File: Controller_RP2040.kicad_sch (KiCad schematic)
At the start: 9 parts, among them J2 Conn_ARM_SWD_TagConnect_TC203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, U3 NCP1117-3.3

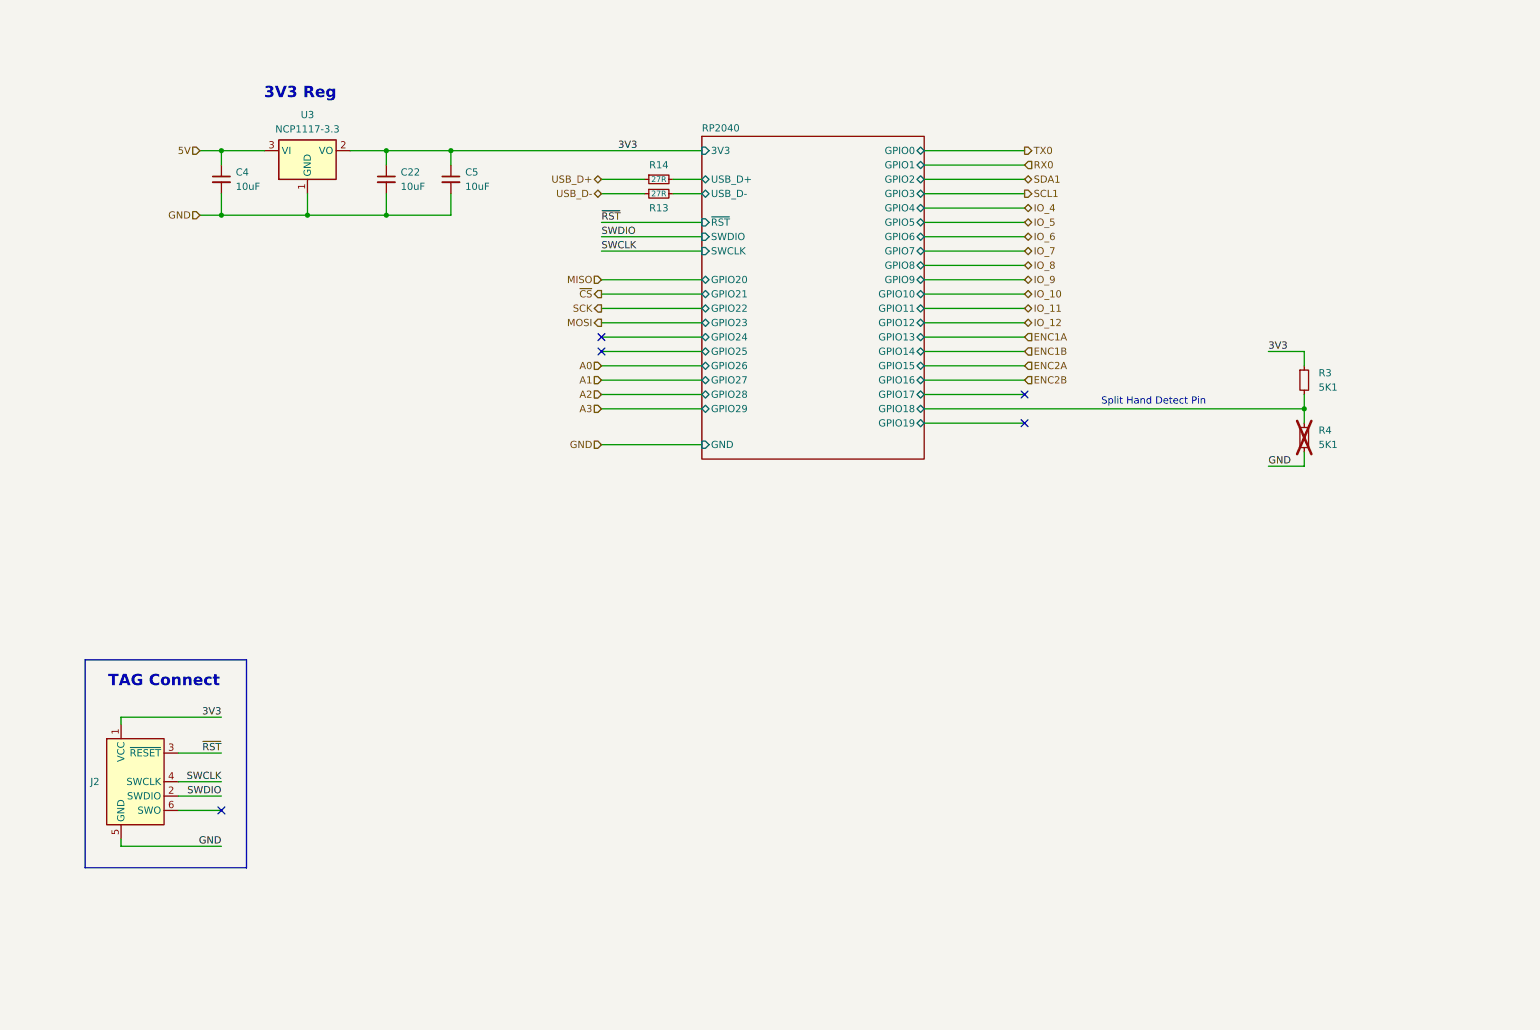
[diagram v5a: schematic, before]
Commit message: Review Schematic, Add TRS connector. Continue routing
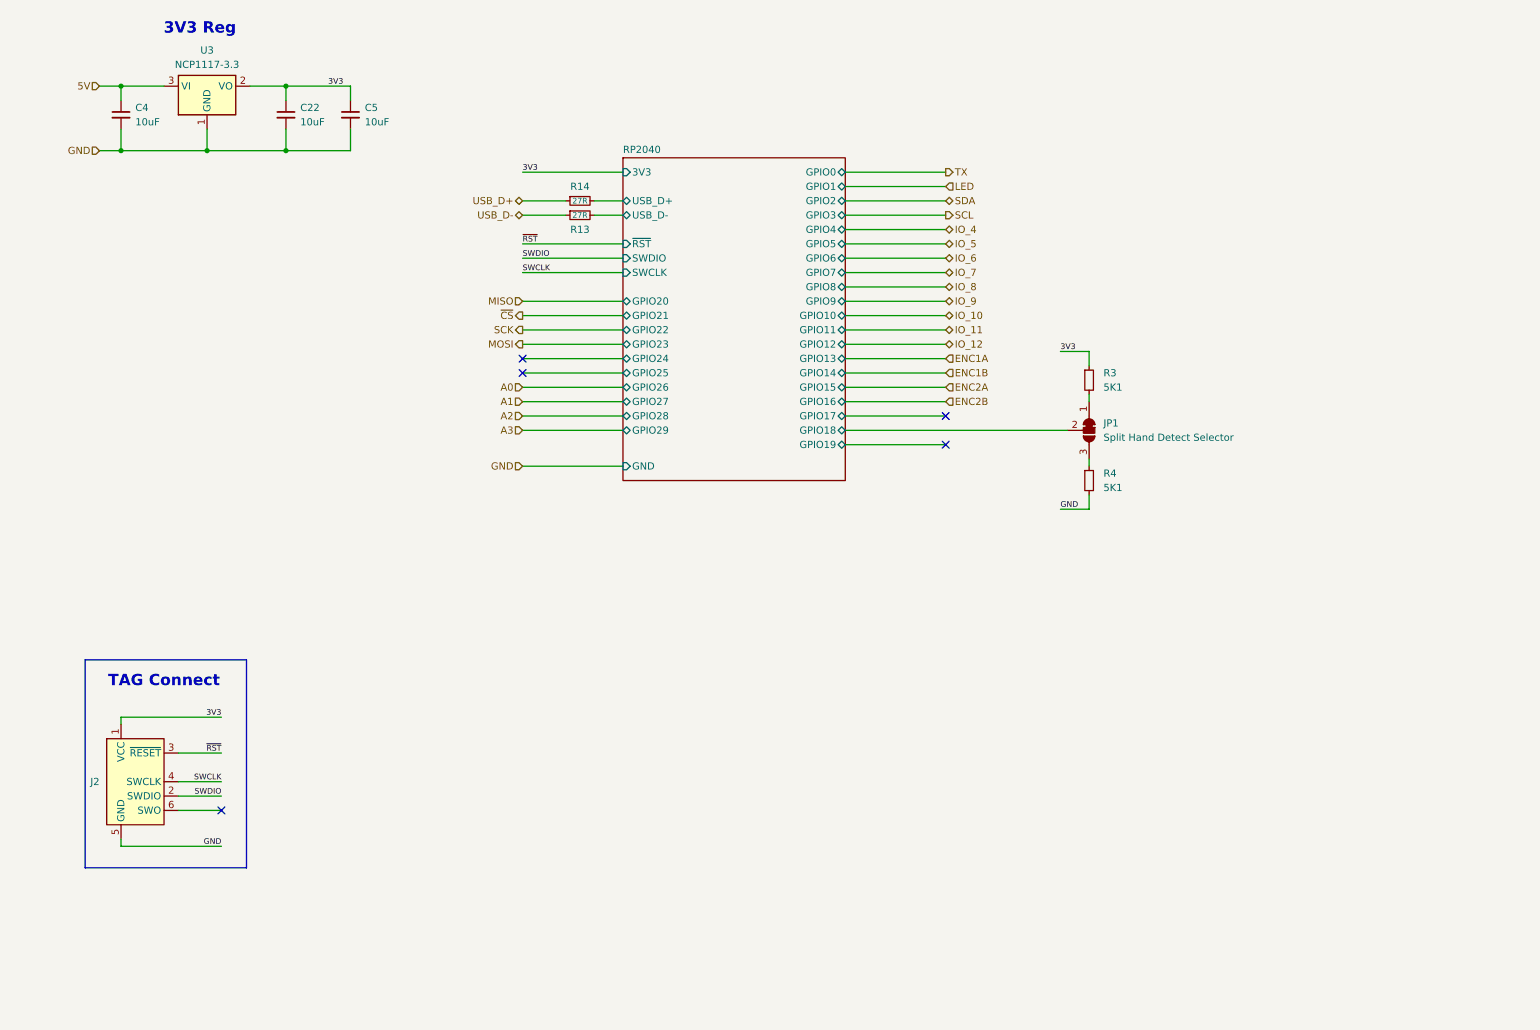
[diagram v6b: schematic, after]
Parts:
- added JP1: Split Hand Detect Selector, Jumper:SolderJumper-3_P1.3mm_Bridged12_RoundedPad1.0x1.5mm, symbol Jumper:SolderJumper_3_Bridged12
- R4: now fitted
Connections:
- net RP2040/GPIO18: now also JP1.2 (C); no longer R3.2, R4.1
- new net: JP1.1 (A), R3.2
- new net: JP1.3 (B), R4.1
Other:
- note removed: "Split Hand Detect Pin"
- moved on the sheet: C22, C4, C5, R13, R14, R3, U3

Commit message: Continue routing.
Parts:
- J2: footprint Connector:Tag-Connect_TC2030-IDC-NL_2x03_P1.27mm_Vertical -> Connector_JST:JST_SHL_SM05B-SHLS-TF_1x05-1MP_P1.00mm_Horizontal; symbol Connector:Conn_ARM_SWD_TagConnect_TC2030-NL -> Connector_Generic_MountingPin:Conn_01x05_MountingPin; now not fitted; now in the parts list
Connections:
- net GND: now also J2.MP (MountPin)
- net SWCLK: now also J2.3 (Pin_3); no longer J2.4 (SWCLK)
- net SWDIO: now also J2.4 (Pin_4); no longer J2.2 (SWDIO)
- net ~{RST}: now also J2.2 (Pin_2); no longer J2.3 (~{RESET})
- no-connect marks 5 -> 4
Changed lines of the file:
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@@
 	(rectangle
 		(start 29.21 132.08)
-		(end 57.785 168.91)
+		(end 57.785 162.56)
 		(stroke
 			(width 0)
@@
 	)
 	(no_connect
-		(at 53.34 158.75)
-	)
-	(no_connect
 		(at 181.61 88.9)
 	)
@@
 	(wire
 		(pts
-			(xy 45.72 156.21) (xy 53.34 156.21)
+			(xy 41.91 149.86) (xy 49.53 149.86)
+		)
+		(stroke
+			(width 0)
+			(type default)
+		)
+	)
+	(wire
+		(pts
+			(xy 36.83 160.02) (xy 48.26 160.02)
 		)
 		(stroke
@@
 	(wire
 		(pts
-			(xy 45.72 153.67) (xy 53.34 153.67)
+			(xy 41.91 147.32) (xy 49.53 147.32)
 		)
 		(stroke
@@
 	(wire
 		(pts
-			(xy 53.34 142.24) (xy 35.56 142.24)
+			(xy 49.53 142.24) (xy 41.91 142.24)
 		)
 		(stroke
@@
 	(wire
 		(pts
+			(xy 41.91 152.4) (xy 49.53 152.4)
+		)
+		(stroke
+			(width 0)
+			(type default)
+		)
+	)
+	(wire
+		(pts
 			(xy 106.68 58.42) (xy 124.46 58.42)
 		)
@@
 	(wire
 		(pts
-			(xy 35.56 142.24) (xy 35.56 143.51)
-		)
-		(stroke
-			(width 0)
-			(type default)
-		)
-	)
-	(wire
-		(pts
 			(xy 35.56 30.48) (xy 35.56 33.02)
 		)
@@
 	(wire
 		(pts
-			(xy 53.34 165.1) (xy 35.56 165.1)
-		)
-		(stroke
-			(width 0)
-			(type default)
-		)
-	)
-	(wire
-		(pts
 			(xy 35.56 30.48) (xy 43.18 30.48)
 		)
@@
 	(wire
 		(pts
-			(xy 45.72 148.59) (xy 53.34 148.59)
+			(xy 41.91 144.78) (xy 49.53 144.78)
 		)
 		(stroke
@@
 	(wire
 		(pts
-			(xy 45.72 158.75) (xy 53.34 158.75)
-		)
-		(stroke
-			(width 0)
-			(type default)
-		)
-	)
-	(wire
-		(pts
 			(xy 163.83 68.58) (xy 181.61 68.58)
 		)
@@
 	(wire
 		(pts
-			(xy 35.56 165.1) (xy 35.56 163.83)
+			(xy 36.83 160.02) (xy 36.83 157.48)
 		)
 		(stroke
@@
 		)
 	)
+	(label "GND"
+		(at 48.26 160.02 180)
+		(effects
+			(font
+				(size 1 1)
+			)
+			(justify right bottom)
+		)
+	)
 	(label "SWDIO"
-		(at 53.34 156.21 180)
+		(at 49.53 149.86 180)
 		(effects
 			(font
@@
 	)
 	(label "~{RST}"
-		(at 53.34 148.59 180)
+		(at 49.53 144.78 180)
 		(effects
 			(font
@@
 	)
 	(label "3V3"
-		(at 53.34 142.24 180)
+		(at 49.53 142.24 180)
 		(effects
 			(font
@@
 	)
 	(label "GND"
-		(at 53.34 165.1 180)
+		(at 49.53 152.4 180)
 		(effects
 			(font
@@
 	)
 	(label "SWCLK"
-		(at 53.34 153.67 180)
+		(at 49.53 147.32 180)
 		(effects
 			(font
@@
 			)
 		)
-		(property "Datasheet" "https://www.yageo.com/upload/media/product/products/datasheet/rchip/PYu-RC_Group_51_RoHS_L_12.pdf"
+		(property "Datasheet" "~"
 			(at 116.84 50.8 0)
 			(effects
@@
 			)
 		)
-		(property "Description" "27 Ohms ±1% 0.063W, 1/16W Chip Resistor 0402 (1005 Metric) Moisture Resistant Thick Film"
+		(property "Description" "Resistor, small symbol"
 			(at 116.84 50.8 0)
 			(effects
@@
 	)
 	(symbol
-		(lib_id "Connector:Conn_ARM_SWD_TagConnect_TC2030-NL")
-		(at 38.1 153.67 0)
+		(lib_id "Connector_Generic_MountingPin:Conn_01x05_MountingPin")
+		(at 36.83 147.32 0)
+		(mirror y)
 		(unit 1)
 		(exclude_from_sim no)
-		(in_bom no)
+		(in_bom yes)
 		(on_board yes)
-		(dnp no)
-		(fields_autoplaced yes)
+		(dnp yes)
 		(property "Reference" "J2"
-			(at 31.75 153.6699 0)
+			(at 34.29 147.3199 0)
+			(effects
+				(font
+					(size 1.27 1.27)
+				)
+				(justify left)
+			)
+		)
+		(property "Value" "Conn_ARM_SWD_TagConnect_TC2030-NL"
+			(at 43.18 148.59 0)
 			(effects
 				(font
@@
 				)
 				(justify right)
-			)
-		)
-		(property "Value" "Conn_ARM_SWD_TagConnect_TC2030-NL"
-			(at 31.75 154.94 0)
-			(effects
-				(font
-					(size 1.27 1.27)
-				)
-				(justify right)
-				(hide yes)
-			)
-		)
-		(property "Footprint" "Connector:Tag-Connect_TC2030-IDC-NL_2x03_P1.27mm_Vertical"
-			(at 38.1 171.45 0)
-			(effects
-				(font
-					(size 1.27 1.27)
-				)
-				(hide yes)
-			)
-		)
-		(property "Datasheet" "https://www.tag-connect.com/wp-content/uploads/bsk-pdf-manager/TC2030-CTX_1.pdf"
-			(at 38.1 168.91 0)
-			(effects
-				(font
-					(size 1.27 1.27)
-				)
-				(hide yes)
-			)
-		)
-		(property "Description" ""
-			(at 38.1 153.67 0)
+				(hide yes)
+			)
+		)
+		(property "Footprint" "Connector_JST:JST_SHL_SM05B-SHLS-TF_1x05-1MP_P1.00mm_Horizontal"
+			(at 36.83 147.32 0)
+			(effects
+				(font
+					(size 1.27 1.27)
+				)
+				(hide yes)
+			)
+		)
+		(property "Datasheet" "~"
+			(at 36.83 147.32 0)
+			(effects
+				(font
+					(size 1.27 1.27)
+				)
+				(hide yes)
+			)
+		)
+		(property "Description" "Generic connectable mounting pin connector, single row, 01x05, script generated (kicad-library-utils/schlib/autogen/connector/)"
+			(at 36.83 147.32 0)
 			(effects
 				(font
@@
 		)
 		(property "Substitute" ""
-			(at 38.1 153.67 0)
+			(at 36.83 147.32 0)
 			(effects
 				(font
@@
 		)
 		(property "Price" ""
-			(at 38.1 153.67 0)
+			(at 36.83 147.32 0)
 			(effects
 				(font
@@
 		)
 		(property "Interface" ""
-			(at 38.1 153.67 0)
+			(at 36.83 147.32 0)
 			(effects
 				(font
@@
 		)
 		(property "Rating" ""
-			(at 38.1 153.67 0)
+			(at 36.83 147.32 0)
 			(effects
 				(font
@@
 		)
 		(property "Supplier" ""
-			(at 38.1 153.67 0)
+			(at 36.83 147.32 0)
 			(effects
 				(font
@@
 		)
 		(property "Supplier PN" ""
-			(at 38.1 153.67 0)
+			(at 36.83 147.32 0)
 			(effects
 				(font
@@
 		)
 		(property "Manufacturer" ""
-			(at 38.1 153.67 0)
+			(at 36.83 147.32 0)
 			(effects
 				(font
@@
 		)
 		(property "MPN" ""
-			(at 38.1 153.67 0)
+			(at 36.83 147.32 0)
 			(effects
 				(font
@@
 		)
 		(property "LCSC" ""
-			(at 38.1 153.67 0)
+			(at 36.83 147.32 0)
 			(effects
 				(font
@@
 		)
 		(property "LCSC PN" ""
-			(at 38.1 153.67 0)
-			(effects
-				(font
-					(size 1.27 1.27)
-				)
+			(at 36.83 147.32 0)
+			(effects
+				(font
+					(size 1.27 1.27)
+				)
+			)
+		)
+		(property "Config" ""
+			(at 36.83 147.32 0)
+			(effects
+				(font
+					(size 1.27 1.27)
+				)
+				(hide yes)
 			)
 		)
@@
 		(pin "5"
 		)
-		(pin "6"
+		(pin "MP"
 		)
 		(instances
@@
 			)
 		)
-		(property "Datasheet" "https://www.yageo.com/upload/media/product/products/datasheet/rchip/PYu-RC_Group_51_RoHS_L_12.pdf"
+		(property "Datasheet" "~"
 			(at 116.84 53.34 0)
 			(effects
@@
 			)
 		)
-		(property "Description" "27 Ohms ±1% 0.063W, 1/16W Chip Resistor 0402 (1005 Metric) Moisture Resistant Thick Film"
+		(property "Description" "Resistor, small symbol"
 			(at 116.84 53.34 0)
 			(effects
@@
 			)
 		)
-		(property "Datasheet" "https://www.yageo.com/upload/media/product/products/datasheet/rchip/PYu-RC_Group_51_RoHS_L_12.pdf"
+		(property "Datasheet" "~"
 			(at 207.01 100.33 0)
 			(effects
@@
 			)
 		)
-		(property "Description" "5.1 kOhms ±1% 0.063W, 1/16W Chip Resistor 0402 (1005 Metric) Moisture Resistant Thick Film"
+		(property "Description" "Resistor, small symbol"
 			(at 207.01 100.33 0)
 			(effects
@@
 			)
 		)
-		(property "Datasheet" "https://www.yageo.com/upload/media/product/products/datasheet/rchip/PYu-RC_Group_51_RoHS_L_12.pdf"
+		(property "Datasheet" "~"
 			(at 207.01 82.55 0)
 			(effects
@@
 			)
 		)
-		(property "Description" "5.1 kOhms ±1% 0.063W, 1/16W Chip Resistor 0402 (1005 Metric) Moisture Resistant Thick Film"
+		(property "Description" "Resistor, small symbol"
 			(at 207.01 82.55 0)
 			(effects
